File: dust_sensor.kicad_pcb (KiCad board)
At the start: 2 copper layers, 50 x 45 mm, 32 parts, among them P1 ADC, P10 PWR, P2 POWER, P3 LCD, P4 LCD_RST, P5 SERIAL, P6 DHT, P7 SENSOR, P8 GPIOS, P9 DEEP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

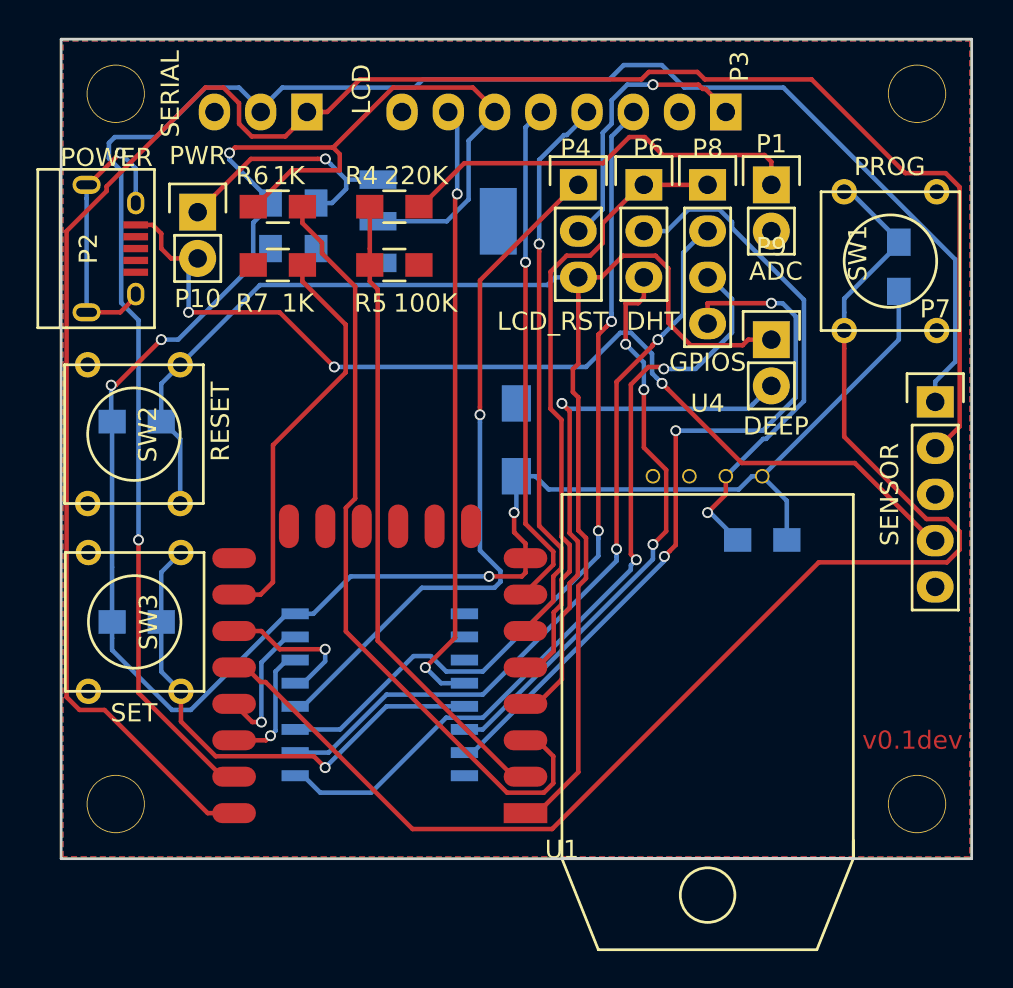
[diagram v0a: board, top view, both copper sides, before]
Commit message: PCB: connect unconnected GNDs
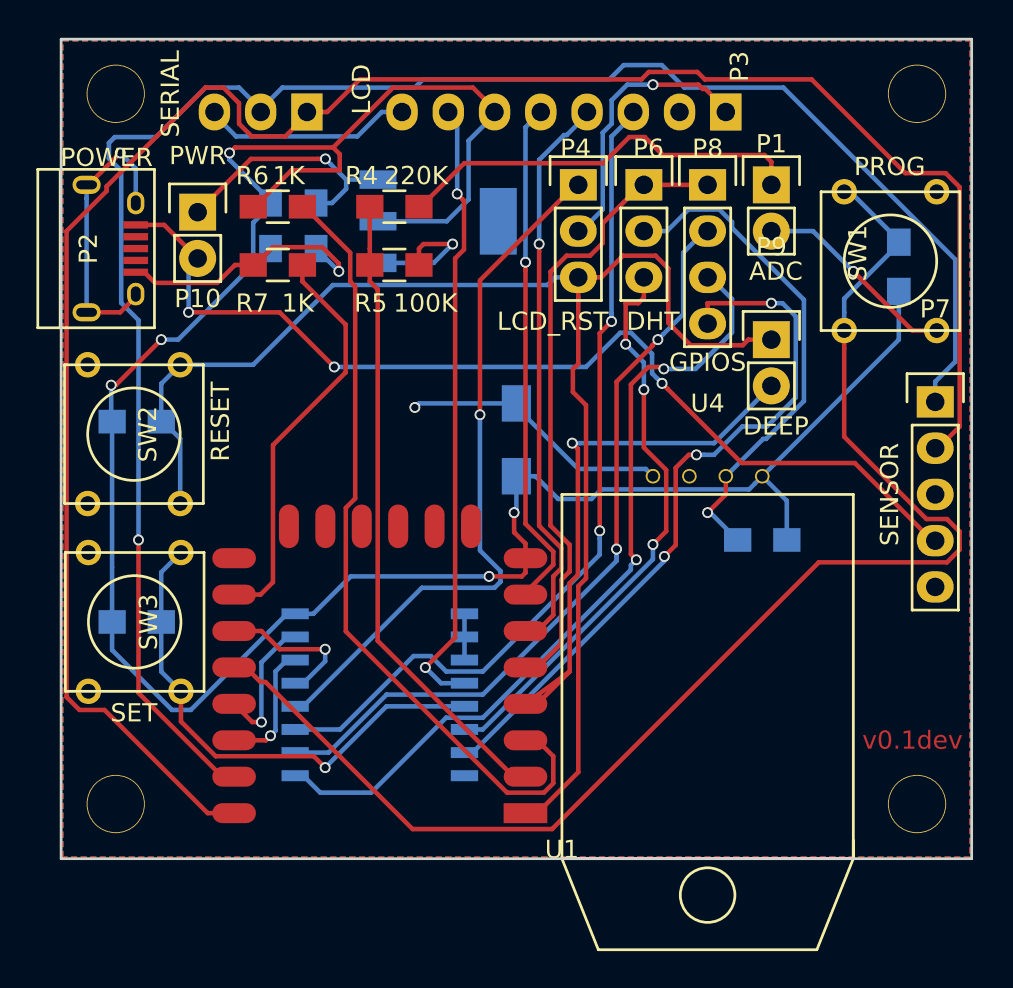
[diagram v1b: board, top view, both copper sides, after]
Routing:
- net GND: track 0.00 -> 62.6 mm, vias 0 -> 4
- net P3: track 40.8 -> 39.6 mm
- net GPIO16: track 30.6 -> 31.3 mm

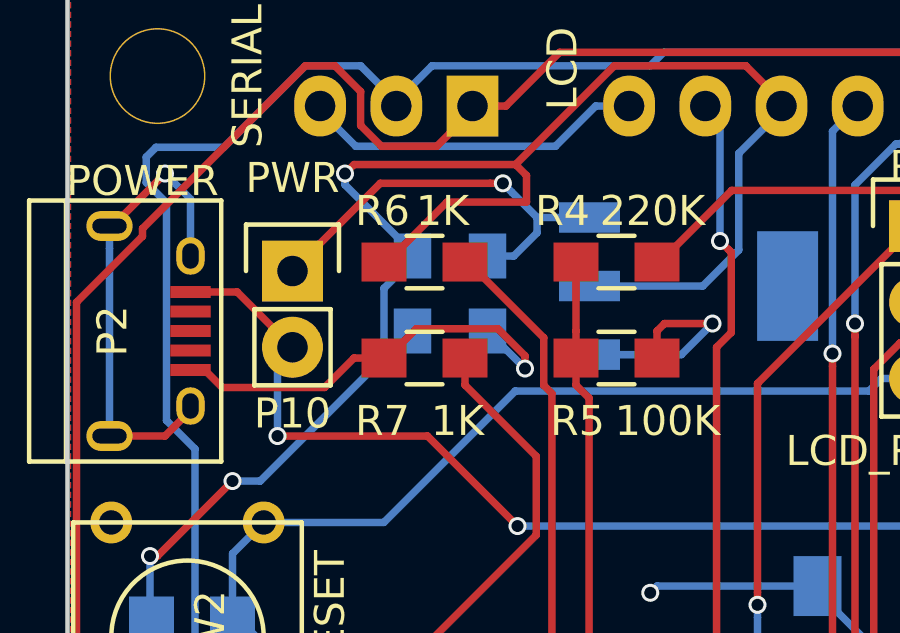
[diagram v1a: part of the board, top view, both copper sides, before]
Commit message: SCH, PCB: Change CH_PD and GPIO15 resistors to 10k
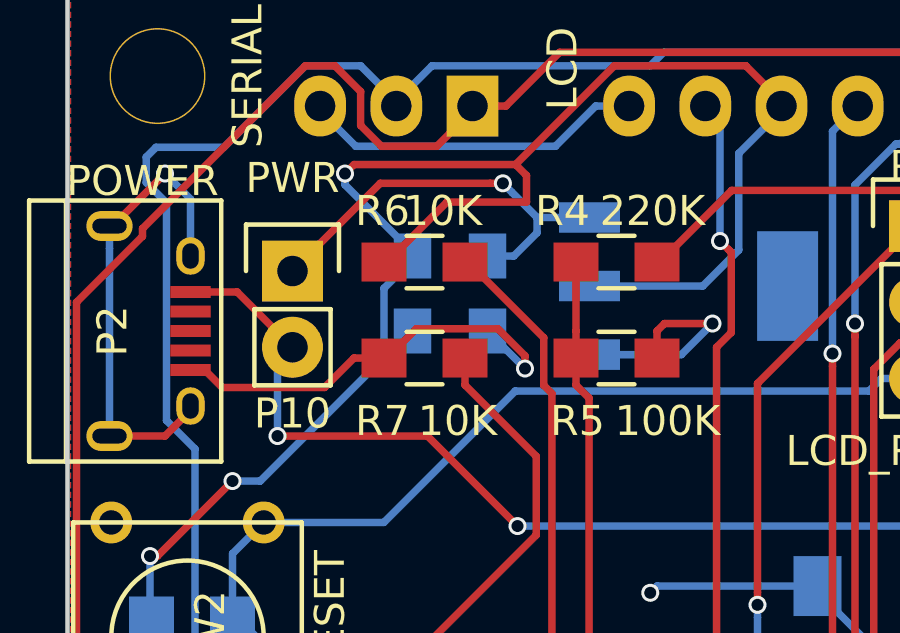
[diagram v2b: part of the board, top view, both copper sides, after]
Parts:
- R6, R7: value 1K -> 10K
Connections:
- P2 pad 2: (no net) -> Net-(P2-Pad2)
- P2 pad 3: (no net) -> Net-(P2-Pad3)
- P2 pad 4: (no net) -> Net-(P2-Pad4)
- P7 pad 5: (no net) -> Net-(P7-Pad5)
- U1 pad 10: (no net) -> Net-(U1-Pad10)
- U1 pad 11: (no net) -> Net-(U1-Pad11)
- U1 pad 12: (no net) -> Net-(U1-Pad12)
- U1 pad 13: (no net) -> Net-(U1-Pad13)
- U1 pad 14: (no net) -> Net-(U1-Pad14)
- U1 pad 9: (no net) -> Net-(U1-Pad9)
- U4 pad 3: (no net) -> Net-(U4-Pad3)
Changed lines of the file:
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@@
     (links 79)
     (no_connects 0)
-    (area 37.762459 24.124999 89.575001 82.176201)
+    (area 39.424999 30.924999 89.575001 76.075001)
     (thickness 1.6)
     (drawings 5)
@@
     (zones 0)
     (modules 32)
-    (nets 31)
+    (nets 42)
   )
   (page A4)
@@
   (net 29 GPIO16)
   (net 30 "Net-(C2-Pad1)")
+  (net 31 "Net-(P2-Pad2)")
+  (net 32 "Net-(P2-Pad3)")
+  (net 33 "Net-(P2-Pad4)")
+  (net 34 "Net-(P7-Pad5)")
+  (net 35 "Net-(U1-Pad9)")
+  (net 36 "Net-(U1-Pad10)")
+  (net 37 "Net-(U1-Pad11)")
+  (net 38 "Net-(U1-Pad12)")
+  (net 39 "Net-(U1-Pad13)")
+  (net 40 "Net-(U1-Pad14)")
+  (net 41 "Net-(U4-Pad3)")
   (net_class Default "This is the default net class."
     (clearance 0.2)
@@
     (add_net "Net-(C2-Pad1)")
     (add_net "Net-(P1-Pad1)")
+    (add_net "Net-(P2-Pad2)")
+    (add_net "Net-(P2-Pad3)")
+    (add_net "Net-(P2-Pad4)")
     (add_net "Net-(P2-Pad6)")
     (add_net "Net-(P3-Pad1)")
@@
     (add_net "Net-(P4-Pad1)")
     (add_net "Net-(P6-Pad2)")
+    (add_net "Net-(P7-Pad5)")
     (add_net "Net-(R6-Pad1)")
     (add_net "Net-(R7-Pad1)")
+    (add_net "Net-(U1-Pad10)")
+    (add_net "Net-(U1-Pad11)")
+    (add_net "Net-(U1-Pad12)")
+    (add_net "Net-(U1-Pad13)")
+    (add_net "Net-(U1-Pad14)")
     (add_net "Net-(U1-Pad17)")
     (add_net "Net-(U1-Pad19)")
     (add_net "Net-(U1-Pad20)")
+    (add_net "Net-(U1-Pad9)")
+    (add_net "Net-(U4-Pad3)")
     (add_net P3)
     (add_net P4)
@@
     (pad 1 smd rect (at -1.3009 -1.56254) (size 1.35 0.4) (layers F.Cu F.Paste F.Mask)
       (net 3 +5V))
-    (pad 2 smd rect (at -0.6509 -1.56254) (size 1.35 0.4) (layers F.Cu F.Paste F.Mask))
-    (pad 3 smd rect (at -0.0009 -1.56254) (size 1.35 0.4) (layers F.Cu F.Paste F.Mask))
-    (pad 4 smd rect (at 0.6491 -1.56254) (size 1.35 0.4) (layers F.Cu F.Paste F.Mask))
+    (pad 2 smd rect (at -0.6509 -1.56254) (size 1.35 0.4) (layers F.Cu F.Paste F.Mask)
+      (net 31 "Net-(P2-Pad2)"))
+    (pad 3 smd rect (at -0.0009 -1.56254) (size 1.35 0.4) (layers F.Cu F.Paste F.Mask)
+      (net 32 "Net-(P2-Pad3)"))
+    (pad 4 smd rect (at 0.6491 -1.56254) (size 1.35 0.4) (layers F.Cu F.Paste F.Mask)
+      (net 33 "Net-(P2-Pad4)"))
     (pad 5 smd rect (at 1.2991 -1.56254) (size 1.35 0.4) (layers F.Cu F.Paste F.Mask)
       (net 2 GND))
@@
     (pad 4 thru_hole oval (at 0 7.62) (size 2.032 1.7272) (drill 1.016) (layers *.Cu *.Mask F.SilkS)
       (net 3 +5V))
-    (pad 5 thru_hole oval (at 0 10.16) (size 2.032 1.7272) (drill 1.016) (layers *.Cu *.Mask F.SilkS))
+    (pad 5 thru_hole oval (at 0 10.16) (size 2.032 1.7272) (drill 1.016) (layers *.Cu *.Mask F.SilkS)
+      (net 34 "Net-(P7-Pad5)"))
     (model Pin_Headers.3dshapes/Pin_Header_Straight_1x05.wrl
       (at (xyz 0 -0.2 0))
@@
       (effects (font (size 1 1) (thickness 0.15)))
     )
-    (fp_text value 1K (at -0.6 1.7 180) (layer F.SilkS)
+    (fp_text value 10K (at -0.6 1.7 180) (layer F.SilkS)
       (effects (font (size 1 1) (thickness 0.15)))
     )
@@
       (effects (font (size 1 1) (thickness 0.15)))
     )
-    (fp_text value 1K (at -1.1 -2.1 180) (layer F.SilkS)
+    (fp_text value 10K (at -1.1 -2.1 180) (layer F.SilkS)
       (effects (font (size 1 1) (thickness 0.15)))
     )
@@
     (fp_line (start 0 15.6) (end 0 -8.4) (layer F.Fab) (width 0.1524))
     (fp_line (start 0 -8.4) (end 16 -8.4) (layer F.Fab) (width 0.1524))
-    (pad 9 smd oval (at 2.99 15.75 270) (size 2.4 1.1) (layers F.Cu F.Paste F.Mask))
-    (pad 10 smd oval (at 4.99 15.75 270) (size 2.4 1.1) (layers F.Cu F.Paste F.Mask))
-    (pad 11 smd oval (at 6.99 15.75 270) (size 2.4 1.1) (layers F.Cu F.Paste F.Mask))
-    (pad 12 smd oval (at 8.99 15.75 270) (size 2.4 1.1) (layers F.Cu F.Paste F.Mask))
-    (pad 13 smd oval (at 10.99 15.75 270) (size 2.4 1.1) (layers F.Cu F.Paste F.Mask))
-    (pad 14 smd oval (at 12.99 15.75 270) (size 2.4 1.1) (layers F.Cu F.Paste F.Mask))
+    (pad 9 smd oval (at 2.99 15.75 270) (size 2.4 1.1) (layers F.Cu F.Paste F.Mask)
+      (net 35 "Net-(U1-Pad9)"))
+    (pad 10 smd oval (at 4.99 15.75 270) (size 2.4 1.1) (layers F.Cu F.Paste F.Mask)
+      (net 36 "Net-(U1-Pad10)"))
+    (pad 11 smd oval (at 6.99 15.75 270) (size 2.4 1.1) (layers F.Cu F.Paste F.Mask)
+      (net 37 "Net-(U1-Pad11)"))
+    (pad 12 smd oval (at 8.99 15.75 270) (size 2.4 1.1) (layers F.Cu F.Paste F.Mask)
+      (net 38 "Net-(U1-Pad12)"))
+    (pad 13 smd oval (at 10.99 15.75 270) (size 2.4 1.1) (layers F.Cu F.Paste F.Mask)
+      (net 39 "Net-(U1-Pad13)"))
+    (pad 14 smd oval (at 12.99 15.75 270) (size 2.4 1.1) (layers F.Cu F.Paste F.Mask)
+      (net 40 "Net-(U1-Pad14)"))
     (pad 1 smd rect (at 0 0 180) (size 2.4 1.1) (layers F.Cu F.Paste F.Mask)
       (net 12 RESET))
@@
     (pad 2 thru_hole circle (at -1 -1 180) (size 0.8 0.8) (drill 0.6) (layers *.Cu *.Mask F.SilkS)
       (net 16 "Net-(P6-Pad2)"))
-    (pad 3 thru_hole circle (at 1 -1 180) (size 0.8 0.8) (drill 0.6) (layers *.Cu *.Mask F.SilkS))
+    (pad 3 thru_hole circle (at 1 -1 180) (size 0.8 0.8) (drill 0.6) (layers *.Cu *.Mask F.SilkS)
+      (net 41 "Net-(U4-Pad3)"))
     (pad 4 thru_hole circle (at 3 -1 180) (size 0.8 0.8) (drill 0.6) (layers *.Cu *.Mask F.SilkS)
       (net 2 GND))

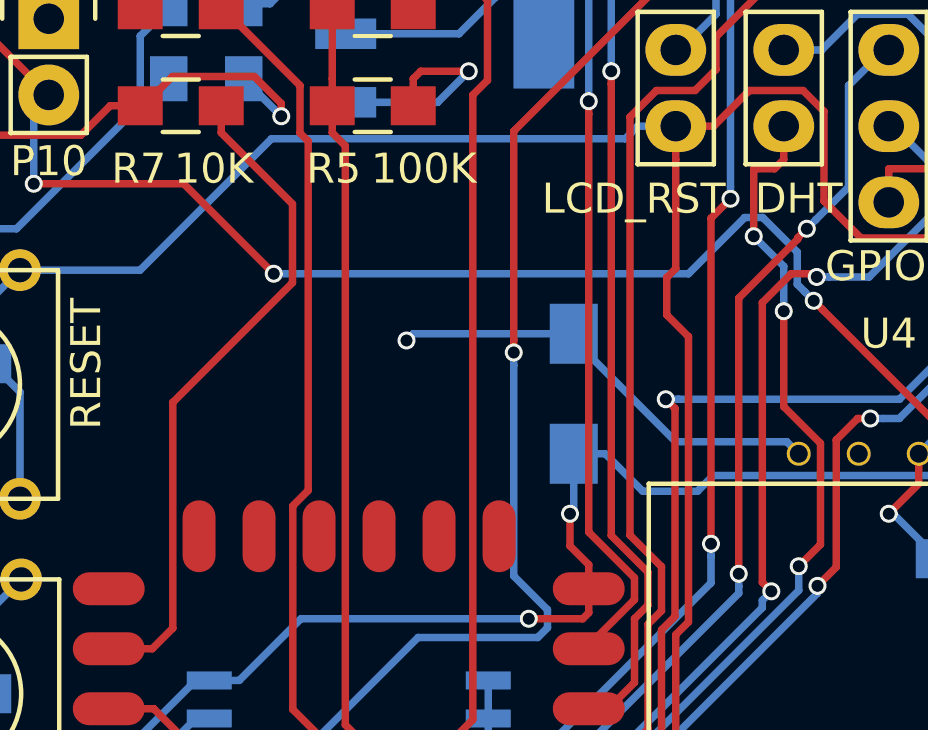
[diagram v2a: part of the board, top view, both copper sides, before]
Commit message: Use tantalum footprint for 100uF capacitor.
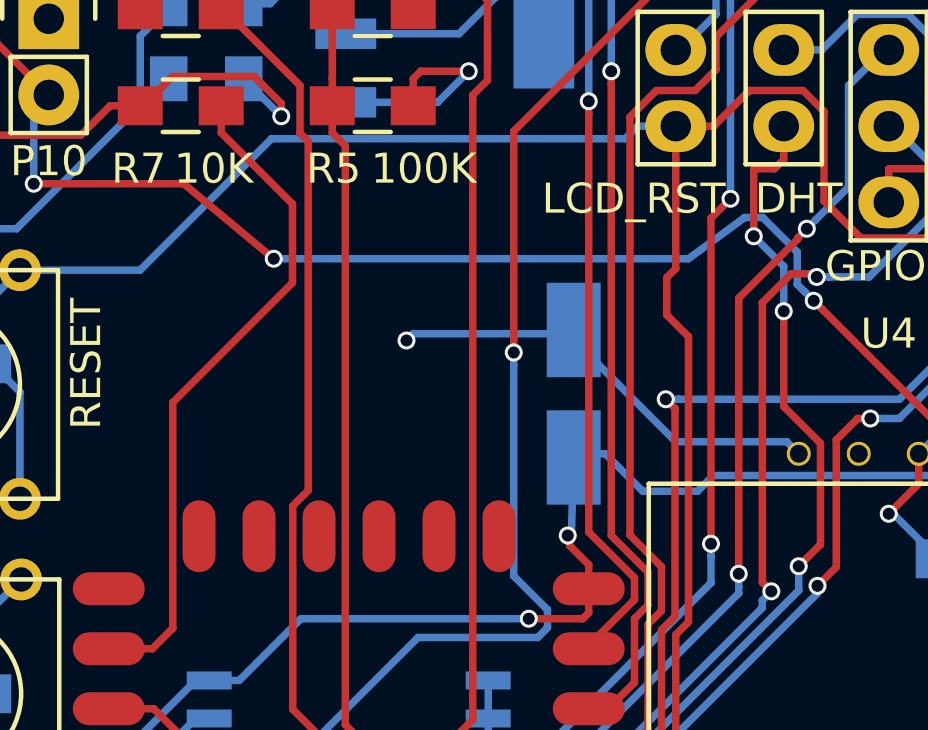
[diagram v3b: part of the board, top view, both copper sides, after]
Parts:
- C1: footprint Capacitors_SMD:C_1206_HandSoldering -> Capacitors_Tantalum_SMD:TantalC_SizeB_EIA-3528_HandSoldering
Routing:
- net +5V: track 56.5 -> 55.8 mm
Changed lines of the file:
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@@
     (add_net TX)
-  )
-  (module Capacitors_SMD:C_1206_HandSoldering (layer B.Cu)
-    (at 64.5 53 90)
-    (descr "Capacitor SMD 1206, hand soldering")
-    (tags "capacitor 1206")
-    (attr smd)
-    (fp_text reference C1 (at 2.75 -2 90) (layer B.SilkS)
-      (effects (font (size 1 1) (thickness 0.15)) (justify mirror))
-    )
-    (fp_text value 100u (at -0.75 -2 90) (layer B.SilkS)
-      (effects (font (size 1 1) (thickness 0.15)) (justify mirror))
-    )
-    (fp_line (start -3.3 1.15) (end 3.3 1.15) (layer B.CrtYd) (width 0.05))
-    (fp_line (start -3.3 -1.15) (end 3.3 -1.15) (layer B.CrtYd) (width 0.05))
-    (fp_line (start -3.3 1.15) (end -3.3 -1.15) (layer B.CrtYd) (width 0.05))
-    (fp_line (start 3.3 1.15) (end 3.3 -1.15) (layer B.CrtYd) (width 0.05))
-    (fp_line (start 1 1.025) (end -1 1.025) (layer B.SilkS) (width 0.15))
-    (fp_line (start -1 -1.025) (end 1 -1.025) (layer B.SilkS) (width 0.15))
-    (pad 1 smd rect (at -2 0 90) (size 2 1.6) (layers B.Cu B.Paste B.Mask)
-      (net 1 +3V3))
-    (pad 2 smd rect (at 2 0 90) (size 2 1.6) (layers B.Cu B.Paste B.Mask)
-      (net 2 GND))
-    (model Capacitors_SMD.3dshapes/C_1206_HandSoldering.wrl
-      (at (xyz 0 0 0))
-      (scale (xyz 1 1 1))
-      (rotate (xyz 0 0 0))
-    )
   )
   (module Capacitors_SMD:C_0805_HandSoldering (layer B.Cu)
@@
     (pad 1 thru_hole circle (at 0 0) (size 3.2 3.2) (drill 3.1) (layers *.Cu *.Mask F.SilkS))
   )
+  (module Capacitors_Tantalum_SMD:TantalC_SizeB_EIA-3528_HandSoldering (layer B.Cu)
+    (at 64.5 53 90)
+    (descr "Tantal Cap. , Size B, EIA-3528, Hand Soldering,")
+    (tags "Tantal Cap. , Size B, EIA-3528, Hand Soldering,")
+    (attr smd)
+    (fp_text reference C1 (at -0.20066 3.29946 90) (layer B.SilkS)
+      (effects (font (size 1 1) (thickness 0.15)) (justify mirror))
+    )
+    (fp_text value 100u (at -0.09906 -3.59918 90) (layer B.Fab)
+      (effects (font (size 1 1) (thickness 0.15)) (justify mirror))
+    )
+    (fp_text user + (at -4.70154 2.4003 90) (layer B.SilkS)
+      (effects (font (size 1 1) (thickness 0.15)) (justify mirror))
+    )
+    (fp_line (start -4.20116 1.89992) (end -4.20116 -1.89992) (layer B.SilkS) (width 0.15))
+    (fp_line (start 2.49936 1.89992) (end -2.49936 1.89992) (layer B.SilkS) (width 0.15))
+    (fp_line (start 2.49682 -1.89992) (end -2.5019 -1.89992) (layer B.SilkS) (width 0.15))
+    (fp_line (start -4.70408 2.90322) (end -4.70408 1.8034) (layer B.SilkS) (width 0.15))
+    (fp_line (start -5.30352 2.40284) (end -4.10464 2.40284) (layer B.SilkS) (width 0.15))
+    (pad 2 smd rect (at 2.12598 0 90) (size 3.1496 1.80086) (layers B.Cu B.Paste B.Mask)
+      (net 2 GND))
+    (pad 1 smd rect (at -2.12598 0 90) (size 3.1496 1.80086) (layers B.Cu B.Paste B.Mask)
+      (net 1 +3V3))
+    (model Capacitors_Tantalum_SMD.3dshapes/TantalC_SizeB_EIA-3528_HandSoldering.wrl
+      (at (xyz 0 0 0))
+      (scale (xyz 1 1 1))
+      (rotate (xyz 0 0 180))
+    )
+  )
   (gr_text v0.1dev (at 86.25 69.5) (layer F.Cu)
     (effects (font (size 1 1) (thickness 0.2)))
@@
   (segment (start 65 58.7) (end 64.37499 58.07499) (width 0.25) (layer F.Cu) (net 1))
   (segment (start 65 59.5) (end 65 58.7) (width 0.25) (layer F.Cu) (net 1))
-  (segment (start 64.5 56.87499) (end 64.37499 57) (width 0.25) (layer B.Cu) (net 1))
-  (segment (start 64.5 55) (end 64.5 56.87499) (width 0.25) (layer B.Cu) (net 1))
-  (via (at 64.37499 57) (size 0.6) (drill 0.4) (layers F.Cu B.Cu) (net 1))
-  (segment (start 64.37499 58.07499) (end 64.37499 57) (width 0.25) (layer F.Cu) (net 1))
+  (segment (start 64.42501 57.59999) (end 64.3 57.725) (width 0.25) (layer B.Cu) (net 1))
+  (segment (start 64.5 55) (end 64.42501 57.59999) (width 0.25) (layer B.Cu) (net 1))
+  (via (at 64.3 57.725) (size 0.6) (drill 0.4) (layers F.Cu B.Cu) (net 1))
+  (segment (start 64.37499 58.07499) (end 64.3 57.725) (width 0.25) (layer F.Cu) (net 1))
   (segment (start 52.35 62.555) (end 51.9 62.555) (width 0.25) (layer B.Cu) (net 1))
   (segment (start 51.9 62.555) (end 46.621499 67.833501) (width 0.25) (layer B.Cu) (net 1))
@@
   (segment (start 47 43.04) (end 45.1591 41.1991) (width 0.25) (layer F.Cu) (net 3))
   (segment (start 45.1591 41.1991) (end 43.6 41.1991) (width 0.25) (layer F.Cu) (net 3))
-  (segment (start 68.324996 49) (end 70.199998 47.124998) (width 0.25) (layer B.Cu) (net 3))
+  (segment (start 68.324996 48.5) (end 70.199998 47.124998) (width 0.25) (layer B.Cu) (net 3))
   (segment (start 72.199025 49.600723) (end 72.499024 49.900722) (width 0.25) (layer B.Cu) (net 3))
   (segment (start 71.950011 48.275007) (end 71.950011 49.351709) (width 0.25) (layer B.Cu) (net 3))
@@
   (segment (start 70.800002 47.124998) (end 71.950011 48.275007) (width 0.25) (layer B.Cu) (net 3))
   (segment (start 71.950011 49.351709) (end 72.199025 49.600723) (width 0.25) (layer B.Cu) (net 3))
-  (segment (start 54.5 49) (end 68.324996 49) (width 0.25) (layer B.Cu) (net 3))
+  (segment (start 54.5 48.5) (end 68.324996 48.5) (width 0.25) (layer B.Cu) (net 3))
   (segment (start 72.799023 50.200721) (end 72.499024 49.900722) (width 0.25) (layer F.Cu) (net 3))
   (segment (start 76.873301 54.274999) (end 72.799023 50.200721) (width 0.25) (layer F.Cu) (net 3))
@@
   (segment (start 46.5 46) (end 46.5 43.54) (width 0.25) (layer B.Cu) (net 3))
   (segment (start 46.5 43.54) (end 47 43.04) (width 0.25) (layer B.Cu) (net 3))
-  (segment (start 54.5 49) (end 51.5 46) (width 0.25) (layer F.Cu) (net 3))
+  (segment (start 54.5 48.5) (end 51.5 46) (width 0.25) (layer F.Cu) (net 3))
   (segment (start 51.5 46) (end 46.5 46) (width 0.25) (layer F.Cu) (net 3))
   (via (at 46.5 46) (size 0.6) (drill 0.4) (layers F.Cu B.Cu) (net 3))
-  (via (at 54.5 49) (size 0.6) (drill 0.4) (layers F.Cu B.Cu) (net 3))
+  (via (at 54.5 48.5) (size 0.6) (drill 0.4) (layers F.Cu B.Cu) (net 3))
   (segment (start 46.29 42.79) (end 47 43.04) (width 0.25) (layer F.Cu) (net 3))
   (segment (start 78.5 37.734) (end 78.5 39) (width 0.25) (layer F.Cu) (net 4))
